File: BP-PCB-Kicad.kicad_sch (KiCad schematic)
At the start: 23 parts, among them J1 Conn_02x25_Odd_Even, J10 A3C-4DA-2DSA_71_, J11 Conn_02x25_Odd_Even, J12 A3C-4DA-2DSA_71_, J15 Conn_02x25_Odd_Even, J16 DF14-15P-1.25H52, J17 DF14-30P-1.25H_35_, J18 DF14-15P-1.25H52, J19 DF14-15P-1.25H52, J20 A3C-50DA-2DSA_71_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

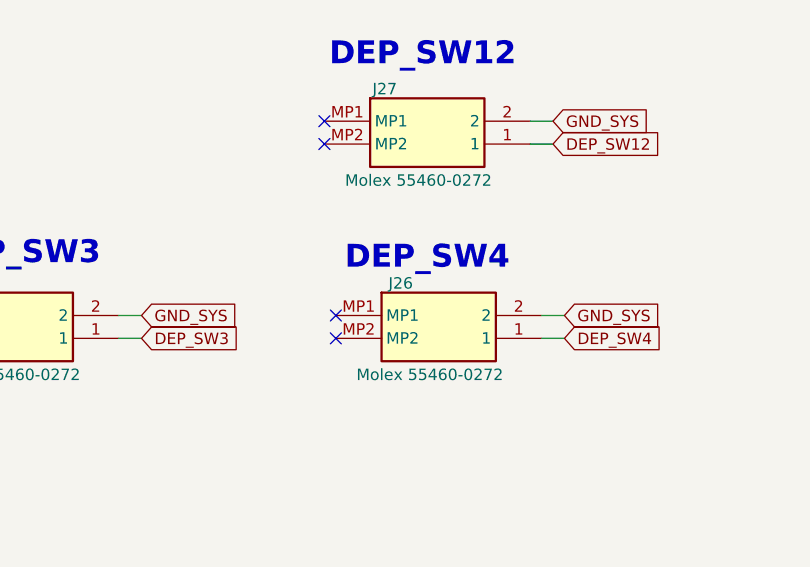
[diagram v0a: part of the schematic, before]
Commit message: Git Submodule added inside <KiCad-Libaries> folder to share libraries across different projects
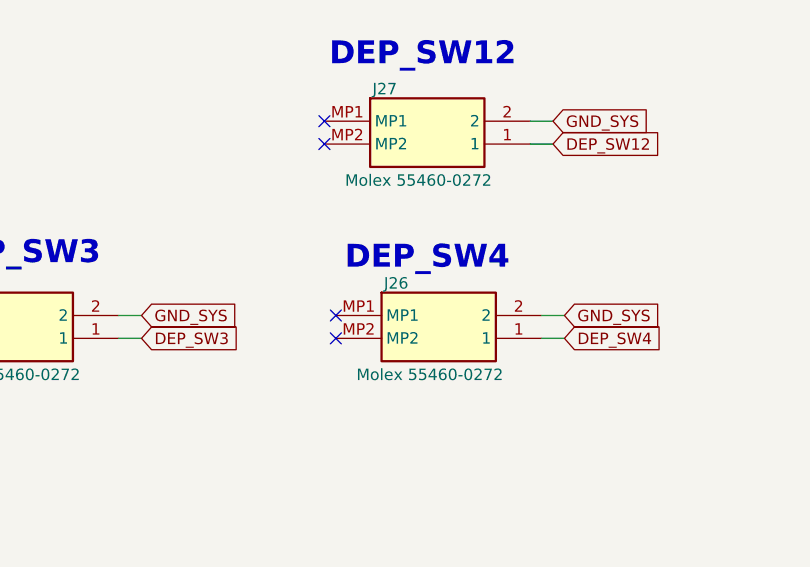
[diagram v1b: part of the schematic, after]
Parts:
- J10: footprint BPB-Footprints:Hirose_A3C-4DA-2DSA(71) -> Custom-Footprints:Hirose_A3C-4DA-2DSA(71); symbol BPB-Symbols:A3C-4DA-2DSA_71_ -> Custom-Symbols:A3C-4DA-2DSA_71_
- J12: footprint BPB-Footprints:Hirose_A3C-4DA-2DSA(71) -> Custom-Footprints:Hirose_A3C-4DA-2DSA(71); symbol BPB-Symbols:A3C-4DA-2DSA_71_FOOTER -> Custom-Symbols:A3C-4DA-2DSA_71_FOOTER
- J16, J18, J19: footprint BPB-Footprints:Hirose_DF14-15P-1.25H(52) -> Custom-Footprints:Hirose_DF14-15P-1.25H(52); symbol BPB-Symbols:DF14-15P-1.25H52 -> Custom-Symbols:DF14-15P-1.25H52
- J17: footprint BPB-Footprints:Hirose_DF14-30P-1.25H(35) -> Custom-Footprints:Hirose_DF14-30P-1.25H(35); symbol BPB-Symbols:DF14-30P-1.25H_35_ -> Custom-Symbols:DF14-30P-1.25H_35_
- J20, J21, J23: footprint BPB-Footprints:Hirose_A3C-50DA-2DSC(71) -> Custom-Footprints:Hirose_A3C-50DA-2DSC(71); symbol BPB-Symbols:A3C-50DA-2DSA_71_ -> Custom-Symbols:A3C-50DA-2DSA_71_
- J22, J24: footprint BPB-Footprints:Hirose_A3C-50DA-2DSC(71)_Mirrored -> Custom-Footprints:Hirose_A3C-50DA-2DSC(71)_Mirrored; symbol BPB-Symbols:A3C-50DA-2DSA_71_ -> Custom-Symbols:A3C-50DA-2DSA_71_
- J25, J26, J27: footprint BPB-Footprints:Molex_0554600272 -> Custom-Footprints:Molex_0554600272; symbol BPB-Symbols:Molex 55460-0272 -> Custom-Symbols:Molex 55460-0272
- J28: footprint BPB-Footprints:PSR-210153-20_P2.00mm -> Custom-Footprints:PSR-210153-20_P2.00mm
- J29: footprint BPB-Footprints:PSR-210153-20_P2.00mm_Mirrored -> Custom-Footprints:PSR-210153-20_P2.00mm_Mirrored
- J7: footprint BPB-Footprints:Hirose_A3C-4DA-2DSA(71)_Mirrored -> Custom-Footprints:Hirose_A3C-4DA-2DSA(71)_Mirrored; symbol BPB-Symbols:A3C-4DA-2DSA_71_ -> Custom-Symbols:A3C-4DA-2DSA_71_
- J9: footprint BPB-Footprints:Hirose_A3C-4DA-2DSA(71)_Mirrored -> Custom-Footprints:Hirose_A3C-4DA-2DSA(71)_Mirrored; symbol BPB-Symbols:A3C-4DA-2DSA_71_FOOTER -> Custom-Symbols:A3C-4DA-2DSA_71_FOOTER
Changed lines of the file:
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@@
 	)
 	(symbol
-		(lib_id "BPB-Symbols:A3C-50DA-2DSA_71_")
+		(lib_id "Custom-Symbols:A3C-50DA-2DSA_71_")
 		(at 168.91 33.02 0)
 		(unit 1)
@@
 			)
 		)
-		(property "Footprint" "BPB-Footprints:Hirose_A3C-50DA-2DSC(71)"
+		(property "Footprint" "Custom-Footprints:Hirose_A3C-50DA-2DSC(71)"
 			(at 187.96 127.94 0)
 			(effects
@@
 	)
 	(symbol
-		(lib_id "BPB-Symbols:DF14-15P-1.25H52")
+		(lib_id "Custom-Symbols:DF14-15P-1.25H52")
 		(at 154.94 234.95 0)
 		(unit 1)
@@
 			)
 		)
-		(property "Footprint" "BPB-Footprints:Hirose_DF14-15P-1.25H(52)"
+		(property "Footprint" "Custom-Footprints:Hirose_DF14-15P-1.25H(52)"
 			(at 163.322 232.918 0)
 			(effects
@@
 	)
 	(symbol
-		(lib_id "BPB-Symbols:Molex 55460-0272")
+		(lib_id "Custom-Symbols:Molex 55460-0272")
 		(at 351.79 237.49 0)
 		(unit 1)
@@
 		(dnp no)
 		(property "Reference" "J26"
-			(at 357.632 233.172 0)
+			(at 357.124 233.172 0)
 			(effects
 				(font
@@
 			)
 		)
-		(property "Footprint" "BPB-Footprints:Molex_0554600272"
+		(property "Footprint" "Custom-Footprints:Molex_0554600272"
 			(at 370.84 332.41 0)
 			(effects
@@
 	)
 	(symbol
-		(lib_id "BPB-Symbols:A3C-50DA-2DSA_71_")
+		(lib_id "Custom-Symbols:A3C-50DA-2DSA_71_")
 		(at 163.83 134.62 0)
 		(unit 1)
@@
 			)
 		)
-		(property "Footprint" "BPB-Footprints:Hirose_A3C-50DA-2DSC(71)_Mirrored"
+		(property "Footprint" "Custom-Footprints:Hirose_A3C-50DA-2DSC(71)_Mirrored"
 			(at 182.88 229.54 0)
 			(effects
@@
 	)
 	(symbol
-		(lib_id "BPB-Symbols:Molex 55460-0272")
+		(lib_id "Custom-Symbols:Molex 55460-0272")
 		(at 304.8 237.49 0)
 		(unit 1)
@@
 			)
 		)
-		(property "Footprint" "BPB-Footprints:Molex_0554600272"
+		(property "Footprint" "Custom-Footprints:Molex_0554600272"
 			(at 323.85 332.41 0)
 			(effects
@@
 			)
 		)
-		(property "Footprint" "BPB-Footprints:PSR-210153-20_P2.00mm_Mirrored"
+		(property "Footprint" "Custom-Footprints:PSR-210153-20_P2.00mm_Mirrored"
 			(at 284.48 255.27 0)
 			(effects
@@
 	)
 	(symbol
-		(lib_id "BPB-Symbols:A3C-50DA-2DSA_71_")
+		(lib_id "Custom-Symbols:A3C-50DA-2DSA_71_")
 		(at 303.53 40.64 0)
 		(unit 1)
@@
 			)
 		)
-		(property "Footprint" "BPB-Footprints:Hirose_A3C-50DA-2DSC(71)_Mirrored"
+		(property "Footprint" "Custom-Footprints:Hirose_A3C-50DA-2DSC(71)_Mirrored"
 			(at 322.58 135.56 0)
 			(effects
@@
 	)
 	(symbol
-		(lib_id "BPB-Symbols:DF14-30P-1.25H_35_")
+		(lib_id "Custom-Symbols:DF14-30P-1.25H_35_")
 		(at 287.02 138.43 0)
 		(unit 1)
@@
 			)
 		)
-		(property "Footprint" "BPB-Footprints:Hirose_DF14-30P-1.25H(35)"
+		(property "Footprint" "Custom-Footprints:Hirose_DF14-30P-1.25H(35)"
 			(at 308.61 233.35 0)
 			(effects
@@
 	)
 	(symbol
-		(lib_id "BPB-Symbols:A3C-50DA-2DSA_71_")
+		(lib_id "Custom-Symbols:A3C-50DA-2DSA_71_")
 		(at 52.07 144.78 0)
 		(unit 1)
@@
 			)
 		)
-		(property "Footprint" "BPB-Footprints:Hirose_A3C-50DA-2DSC(71)"
+		(property "Footprint" "Custom-Footprints:Hirose_A3C-50DA-2DSC(71)"
 			(at 71.12 239.7 0)
 			(effects
@@
 			)
 		)
-		(property "Footprint" "BPB-Footprints:PSR-210153-20_P2.00mm"
+		(property "Footprint" "Custom-Footprints:PSR-210153-20_P2.00mm"
 			(at 227.33 256.54 0)
 			(effects
@@
 	)
 	(symbol
-		(lib_id "BPB-Symbols:DF14-15P-1.25H52")
+		(lib_id "Custom-Symbols:DF14-15P-1.25H52")
 		(at 368.3 139.7 0)
 		(unit 1)
@@
 			)
 		)
-		(property "Footprint" "BPB-Footprints:Hirose_DF14-15P-1.25H(52)"
+		(property "Footprint" "Custom-Footprints:Hirose_DF14-15P-1.25H(52)"
 			(at 376.682 137.668 0)
 			(effects
@@
 	)
 	(symbol
-		(lib_id "BPB-Symbols:A3C-4DA-2DSA_71_FOOTER")
+		(lib_id "Custom-Symbols:A3C-4DA-2DSA_71_FOOTER")
 		(at 304.8 111.76 0)
 		(unit 1)
@@
 			)
 		)
-		(property "Footprint" "BPB-Footprints:Hirose_A3C-4DA-2DSA(71)_Mirrored"
+		(property "Footprint" "Custom-Footprints:Hirose_A3C-4DA-2DSA(71)_Mirrored"
 			(at 321.31 206.68 0)
 			(effects
@@
 	)
 	(symbol
-		(lib_id "BPB-Symbols:A3C-50DA-2DSA_71_")
+		(lib_id "Custom-Symbols:A3C-50DA-2DSA_71_")
 		(at 52.07 31.75 0)
 		(unit 1)
@@
 			)
 		)
-		(property "Footprint" "BPB-Footprints:Hirose_A3C-50DA-2DSC(71)"
+		(property "Footprint" "Custom-Footprints:Hirose_A3C-50DA-2DSC(71)"
 			(at 71.12 126.67 0)
 			(effects
@@
 	)
 	(symbol
-		(lib_id "BPB-Symbols:A3C-4DA-2DSA_71_")
+		(lib_id "Custom-Symbols:A3C-4DA-2DSA_71_")
 		(at 304.8 26.67 0)
 		(unit 1)
@@
 			)
 		)
-		(property "Footprint" "BPB-Footprints:Hirose_A3C-4DA-2DSA(71)_Mirrored"
+		(property "Footprint" "Custom-Footprints:Hirose_A3C-4DA-2DSA(71)_Mirrored"
 			(at 321.31 121.59 0)
 			(effects
@@
 	)
 	(symbol
-		(lib_id "BPB-Symbols:A3C-4DA-2DSA_71_")
+		(lib_id "Custom-Symbols:A3C-4DA-2DSA_71_")
 		(at 53.34 132.08 0)
 		(unit 1)
@@
 			)
 		)
-		(property "Footprint" "BPB-Footprints:Hirose_A3C-4DA-2DSA(71)"
+		(property "Footprint" "Custom-Footprints:Hirose_A3C-4DA-2DSA(71)"
 			(at 69.85 227 0)
 			(effects
@@
 	)
 	(symbol
-		(lib_id "BPB-Symbols:A3C-4DA-2DSA_71_FOOTER")
+		(lib_id "Custom-Symbols:A3C-4DA-2DSA_71_FOOTER")
 		(at 53.34 215.9 0)
 		(unit 1)
@@
 			)
 		)
-		(property "Footprint" "BPB-Footprints:Hirose_A3C-4DA-2DSA(71)"
+		(property "Footprint" "Custom-Footprints:Hirose_A3C-4DA-2DSA(71)"
 			(at 69.85 310.82 0)
 			(effects
@@
 	)
 	(symbol
-		(lib_id "BPB-Symbols:Molex 55460-0272")
+		(lib_id "Custom-Symbols:Molex 55460-0272")
 		(at 350.52 215.9 0)
 		(unit 1)
@@
 			)
 		)
-		(property "Footprint" "BPB-Footprints:Molex_0554600272"
+		(property "Footprint" "Custom-Footprints:Molex_0554600272"
 			(at 369.57 310.82 0)
 			(effects
@@
 	)
 	(symbol
-		(lib_id "BPB-Symbols:DF14-15P-1.25H52")
+		(lib_id "Custom-Symbols:DF14-15P-1.25H52")
 		(at 69.85 234.95 0)
 		(unit 1)
@@
 			)
 		)
-		(property "Footprint" "BPB-Footprints:Hirose_DF14-15P-1.25H(52)"
+		(property "Footprint" "Custom-Footprints:Hirose_DF14-15P-1.25H(52)"
 			(at 78.232 232.918 0)
 			(effects

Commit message: Adjusted to libraries
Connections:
- net DIO Thruster ON/OFF is gone; now on net MUX-Thruster UART_1 (Thruster_to_MainPIC): J19.8
- net Battery_Voltage_Check: now also J21.22; no longer J21.42
- net DIO_Fault_Indicator: now also J19.11, J21.16; no longer J19.10
- net DIO_Thruster_Active: now also J19.10, J21.15; no longer J19.9
- net DIO_Thruster_ON/OFF: now also J19.9
- net DIO_UHF_Antenna_Deploy: now also J21.42; no longer J21.21
- net FSS-M1-ES_SCL: no longer J17.5
- net FSS-M1-ES_SDA: no longer J17.4
- net GND_SYS: now also J19.6
- net MUX-Thruster UART_1 (MainPIC_to_Thruster): now also J19.7; no longer J19.6
- net MUX-Thruster UART_1 (Thruster_to_MainPIC): no longer J19.7
- net OBC-ADB UART_3 (RelayPIC_to_ComPIC): now also J21.21; no longer J21.22
- net SUP_5V_1: no longer J21.15, J21.16
- net SUP_5V_2: no longer J21.25, J21.26
- net SUP_UNREG_2: no longer J21.35, J21.36
- net DIO_HW_Reset: now reaches J21.10
- net DIO_HW_Reset: now also J19.12
- net UART (CCB_to_ADCS): now reaches J24.17
- net UART (CCB_to_ADCS): now also J17.4
- net UART (ADCS_to_CCB): now reaches J24.18
- net UART (ADCS_to_CCB): now also J17.5
- net Thruster_1: now reaches J19.13
- net Thruster_2: now reaches J19.14
- net Thruster_3: now reaches J19.15
- net SUP_SYS renamed SUP_3V3
- new net Thruster-1: J21.25
- new net Thruster-2: J21.26
- new net Thurster_3: J21.35
- no-connect marks 76 -> 69
